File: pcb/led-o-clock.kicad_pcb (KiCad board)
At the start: 2 copper layers, 49 x 35 mm, 26 parts, among them J1 USB_C_Receptacle_USB2.0_16P, J4 Led ring, J5 TX/RX/GND, SW3 IO9_BOOT, SW4 RST, U1 AP7361C-33E, U2 ESP32-C3-WROOM-02

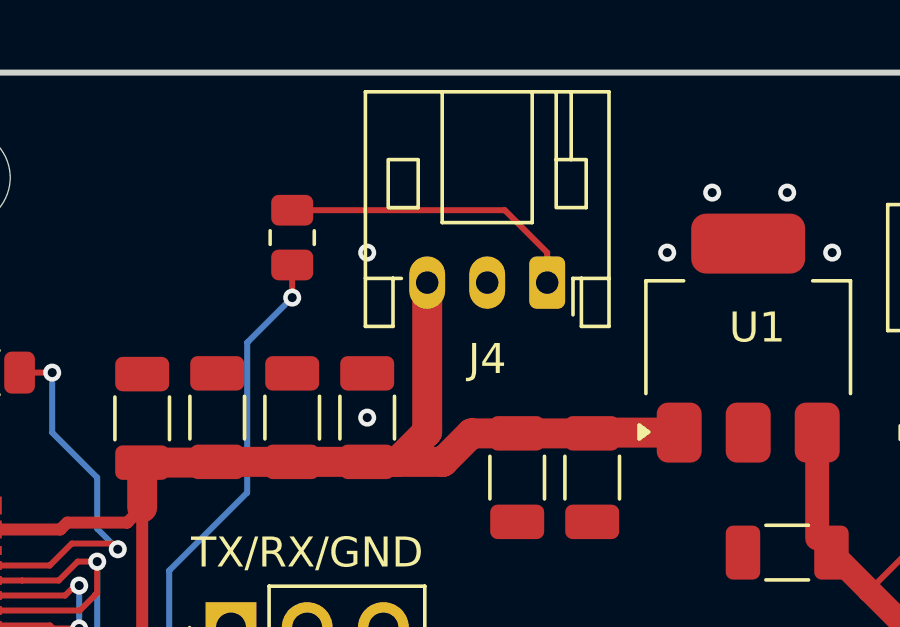
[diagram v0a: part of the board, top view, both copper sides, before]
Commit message: fix(pcb): move jst connector on the top
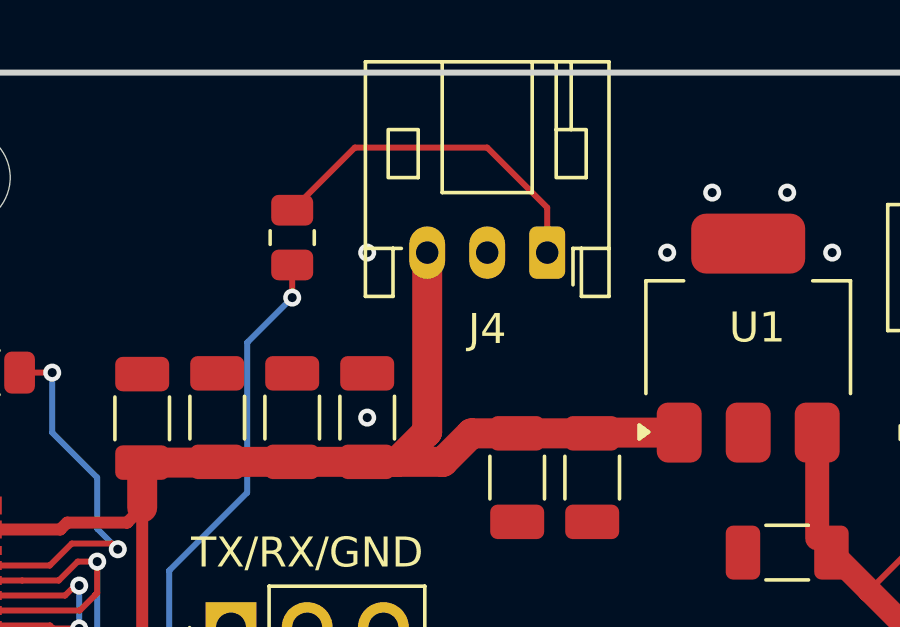
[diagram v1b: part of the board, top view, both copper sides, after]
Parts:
- moved J4 1.00 mm to (145.0, 69.5)
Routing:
- net Net-(J4-Pin_1): track 10.1 -> 11.7 mm
- net /VCC_5V: track 42.2 -> 43.2 mm
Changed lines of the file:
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@@
 	(footprint "Connector_JST:JST_PH_S3B-PH-K_1x03_P2.00mm_Horizontal"
 		(layer "F.Cu")
-		(at 145 70.5 180)
+		(at 145 69.5 180)
 		(descr "JST PH series connector, S3B-PH-K (http://www.jst-mfg.com/product/pdf/eng/ePH.pdf), generated with kicad-footprint-generator")
 		(tags "connector JST PH horizontal")
@@
 	)
 	(segment
-		(start 141 75.475)
-		(end 141 70.5)
-		(width 1)
-		(layer "F.Cu")
-		(net 1)
-	)
-	(segment
 		(start 126.095 78.73)
 		(end 128.77 78.73)
@@
 	)
 	(segment
+		(start 141 75.475)
+		(end 141 69.5)
+		(width 1)
+		(layer "F.Cu")
+		(net 1)
+	)
+	(segment
 		(start 130.42 83.63)
 		(end 126.095 83.63)
@@
 	)
 	(segment
+		(start 140 76.475)
+		(end 141 75.475)
+		(width 1)
+		(layer "F.Cu")
+		(net 1)
+	)
+	(segment
 		(start 141.525 76.475)
 		(end 142.475 75.525)
@@
 		(start 142.475 75.525)
 		(end 144 75.525)
-		(width 1)
-		(layer "F.Cu")
-		(net 1)
-	)
-	(segment
-		(start 140 76.475)
-		(end 141 75.475)
 		(width 1)
 		(layer "F.Cu")
@@
 	(segment
 		(start 136.5 68.0875)
-		(end 143.5875 68.0875)
+		(end 138.5875 66)
 		(width 0.2)
 		(layer "F.Cu")
@@
 	)
 	(segment
-		(start 143.5875 68.0875)
+		(start 138.5875 66)
+		(end 143 66)
+		(width 0.2)
+		(layer "F.Cu")
+		(net 9)
+	)
+	(segment
+		(start 145 68)
 		(end 145 69.5)
 		(width 0.2)
@@
 	)
 	(segment
-		(start 145 69.5)
-		(end 145 70.5)
-		(width 0.2)
-		(layer "F.Cu")
+		(start 143 66)
+		(end 145 68)
+		(width 0.2)
+		(layer "F.Cu")

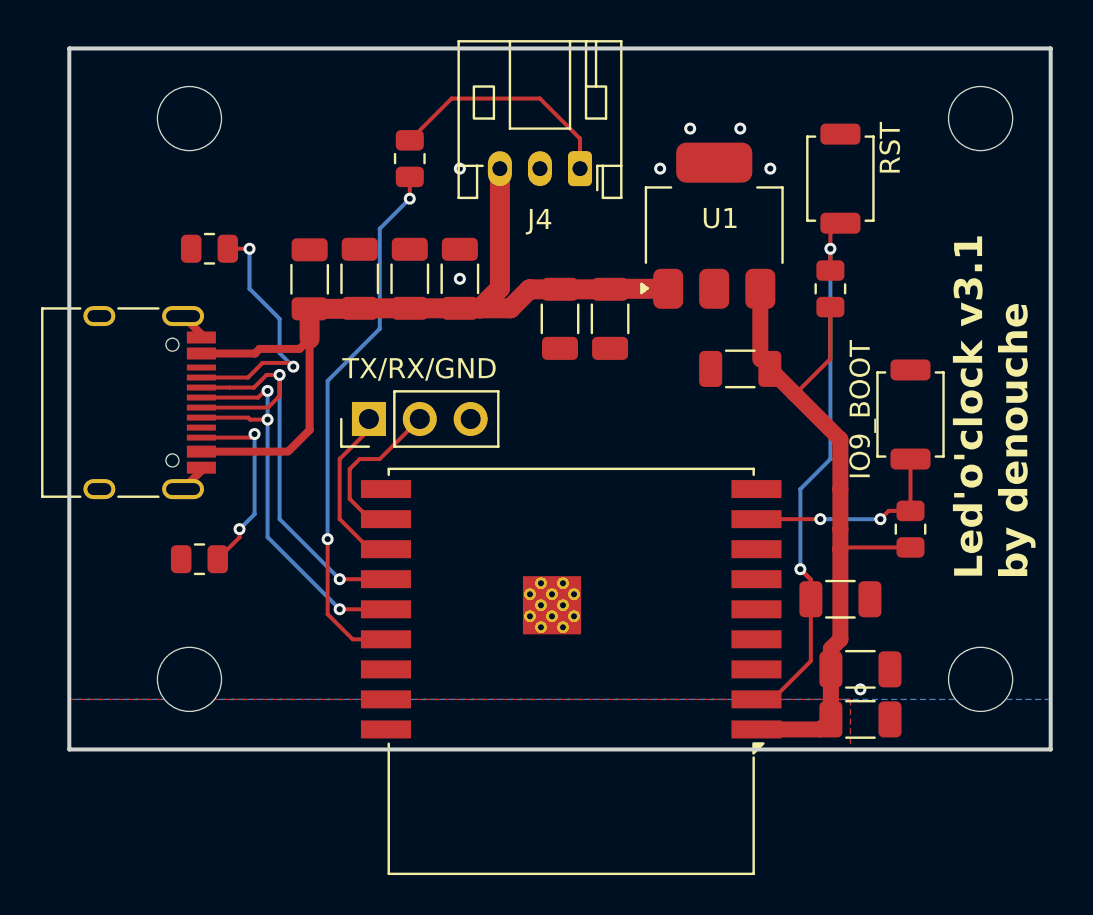
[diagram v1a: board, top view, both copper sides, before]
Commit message: fix(pcb): improve button placement and add QR code
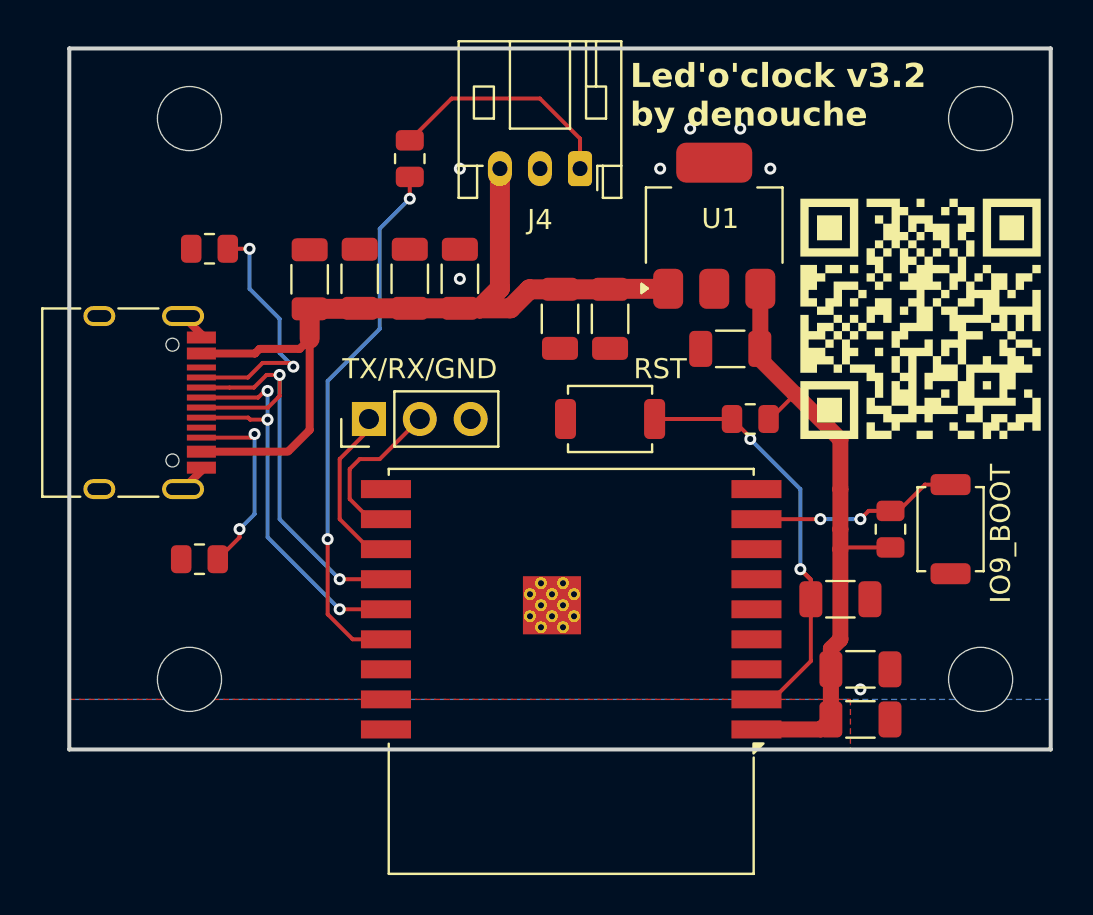
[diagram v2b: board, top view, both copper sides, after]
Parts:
- added G***: LOGO, LOGO, F.Cu at (162.0, 77.0)
- added G***: LOGO, LOGO, B.Cu at (161.0, 77.0)
- moved SW4 16.6 mm to (146.5, 82.0), turned to 0 degrees
- moved R3 7.63 mm to (153.5, 82.0), turned to 0 degrees
- moved SW3 6.06 mm to (163.5, 87.5), turned to 90 degrees
- moved C2 1.12 mm to (152.5, 78.5)
- moved R2 1.00 mm to (160.5, 87.5)
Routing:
- net Net-(U2-EN): track 28.2 -> 21.8 mm
- net /VCC_3.3V: track 35.7 -> 32.1 mm
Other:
- board text added: "Led'o'clock v3.2 by denouche"
- board text removed: "Led'o'clock v3.1 by denouche"

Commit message: feat(pcb): work on v3.2
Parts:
- removed C1, C10, C7, C8, C9: 47uF, Capacitor_SMD:C_1206_3216Metric
- removed J5: TX/RX/GND, Connector_PinHeader_2.54mm:PinHeader_1x03_P2.54mm_Vertical
- added C11: 100uF, Capacitor_SMD:CP_Elec_6.3x5.4, F.Cu at (134.5, 72.5)
- added FB1: FerriteBead_Small, Inductor_SMD:L_0603_1608Metric, F.Cu at (143.5, 75.5)
- moved R4 10.1 mm to (146.0, 72.5), turned to 180 degrees
- moved R1 2.00 mm to (124.5, 73.5)
- moved C3 1.03 mm to (158.0, 97.0)
- moved C6 1.03 mm to (158.0, 94.5)
- moved SW3 1.00 mm to (163.5, 86.5)
- moved C2 0.50 mm to (152.5, 79.0)
- moved SW4 0.50 mm to (147.0, 82.0)
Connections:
- C4 pad 2: /VCC_5V -> Net-(U1-VI)
- U1 pad 1: /VCC_5V -> Net-(U1-VI)
- U2 pad 11: Net-(J5-Pin_2) -> unconnected-(U2-IO20/RXD-Pad11)
- U2 pad 12: Net-(J5-Pin_1) -> unconnected-(U2-IO21/TXD-Pad12)
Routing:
- net Net-(J5-Pin_1): track 8.54 -> 0.00 mm
- net Net-(J5-Pin_2): track 8.26 -> 0.00 mm
- net Net-(J4-Pin_1): track 11.7 -> 4.29 mm
- net Net-(U1-VI): track 0.00 -> 5.12 mm
- net Net-(U2-IO3): track 27.7 -> 31.6 mm
- net /VCC_5V: track 43.2 -> 39.5 mm
- net /VCC_3.3V: track 32.1 -> 31.0 mm
- net Net-(J1-CC1): track 12.9 -> 13.7 mm
- net /GND: vias 7 -> 6
